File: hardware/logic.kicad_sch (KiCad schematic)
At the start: 42 parts, among them J1 Hanrun HY931147C, SW1 SW_Push, U4 ESP32-WROOM-32E, U5 AMS1117-3.3, U6 LAN8720A

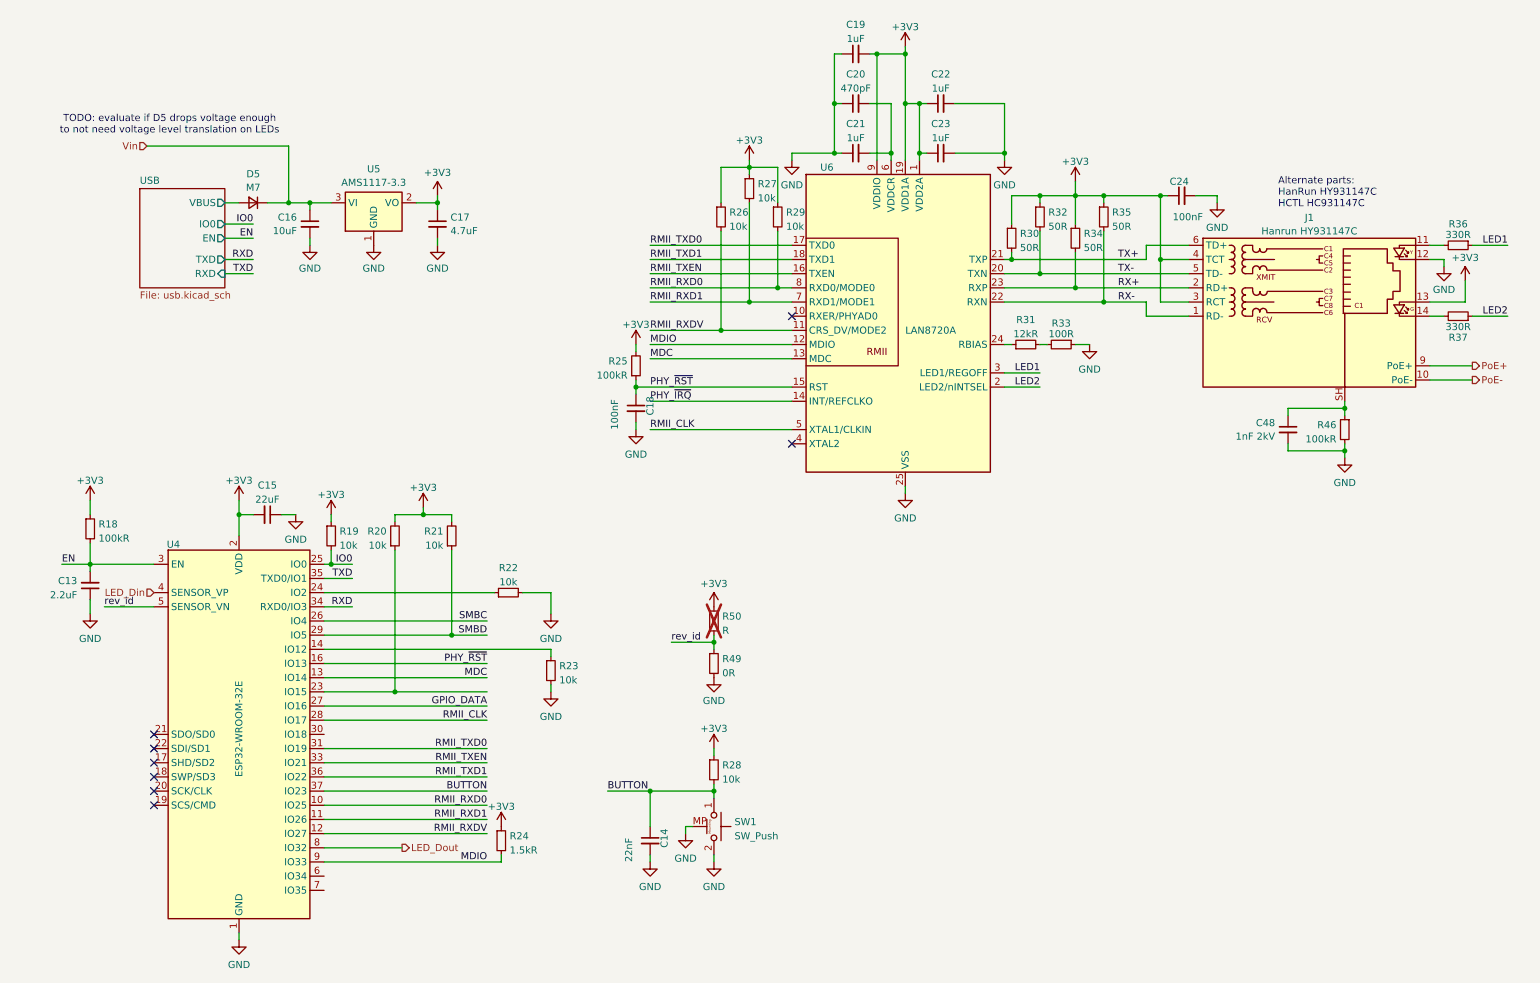
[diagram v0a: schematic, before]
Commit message: hardware: switch to ESP32-C3 MCU and Si3402-B for PoE
Further changes:
 - Enlarge center hole to 16mm diameter
 - Replace Ethernet Phy by KSZ8851 SPI MAC + Phy
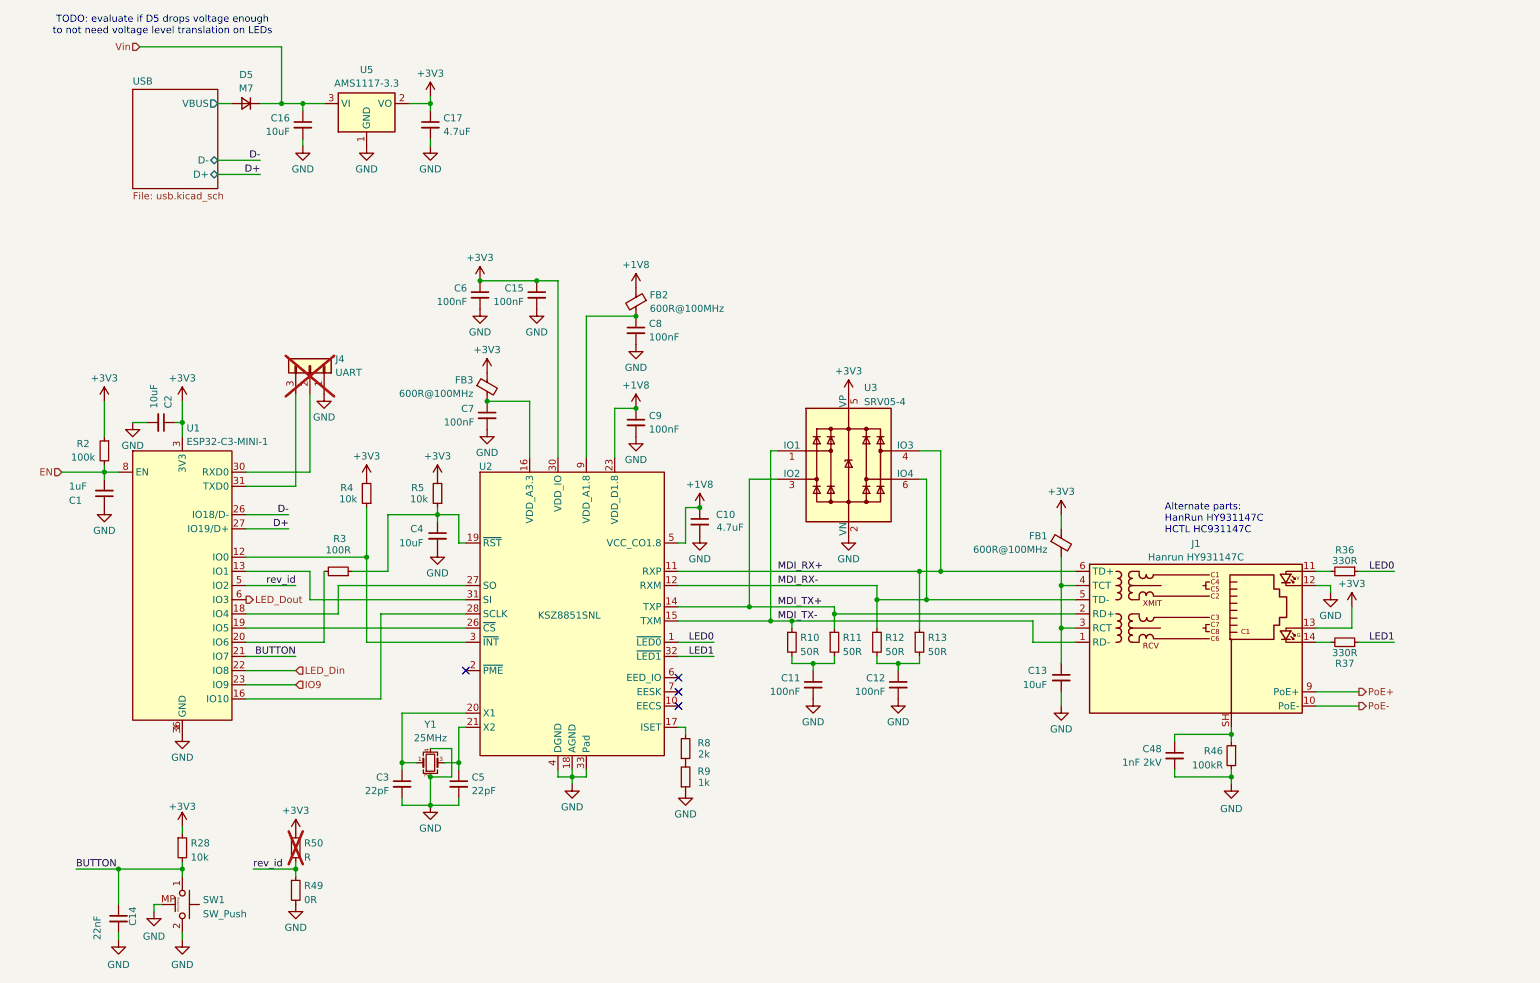
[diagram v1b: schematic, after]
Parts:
- removed C18, C24: 100nF, Capacitor_SMD:C_0402_1005Metric, symbol Device:C_Small
- removed C19, C21, C22, C23: 1uF, Capacitor_SMD:C_0402_1005Metric, symbol Device:C_Small
- removed C20: 470pF, Resistor_SMD:R_0402_1005Metric, symbol Device:C_Small
- removed R18, R25: 100kR, Resistor_SMD:R_0402_1005Metric, symbol Device:R_Small
- removed R19, R20, R21, R22, R23, R26, R27, R29: 10k, Resistor_SMD:R_0402_1005Metric, symbol Device:R_Small
- removed R24: 1.5kR, Resistor_SMD:R_0402_1005Metric, symbol Device:R_Small
- removed R30, R32, R34, R35: 50R, Resistor_SMD:R_0402_1005Metric, symbol Device:R_Small
- removed R31: 12kR, Resistor_SMD:R_0402_1005Metric, symbol Device:R_Small
- removed R33: 100R, Resistor_SMD:R_0402_1005Metric, symbol Device:R_Small
- removed U4: ESP32-WROOM-32E, RF_Module_Espressif:ESP32-WROOM-32E_no_antenna_keepout, symbol RF_Module:ESP32-WROOM-32D
- removed U6: LAN8720A, Package_DFN_QFN:QFN-24-1EP_4x4mm_P0.5mm_EP2.6x2.6mm, symbol Interface_Ethernet:LAN8720A
- added C1: 1uF, Capacitor_SMD:C_0402_1005Metric, symbol Device:C_Small
- added C10: 4.7uF, Capacitor_SMD:C_0402_1005Metric, symbol Device:C_Small
- added C11, C12, C6, C7, C8, C9: 100nF, Capacitor_SMD:C_0402_1005Metric, symbol Device:C_Small
- added C2, C4: 10uF, Capacitor_SMD:C_0402_1005Metric, symbol Device:C_Small
- added C3, C5: 22pF, Capacitor_SMD:C_0402_1005Metric, symbol Device:C_Small
- added FB1, FB2, FB3: 600R@100MHz, Inductor_SMD:L_0402_1005Metric, symbol Device:FerriteBead_Small
- added J4: UART, Connector_PinHeader_2.54mm:PinHeader_1x03_P2.54mm_Vertical, symbol Connector_Generic:Conn_01x03
- added R10, R11, R12, R13: 50R, Resistor_SMD:R_0402_1005Metric, symbol Device:R_Small
- added R2: 100k, Resistor_SMD:R_0402_1005Metric, symbol Device:R_Small
- added R3: 100R, Resistor_SMD:R_0402_1005Metric, symbol Device:R_Small
- added R4, R5: 10k, Resistor_SMD:R_0402_1005Metric, symbol Device:R_Small
- added R8: 2k, Resistor_SMD:R_0402_1005Metric, symbol Device:R_Small
- added R9: 1k, Resistor_SMD:R_0402_1005Metric, symbol Device:R_Small
- added U1: ESP32-C3-MINI-1, ESP32_C3:ESP32-C3-MINI-1, symbol ESP32_C3:ESP32-C3-MINI-1
- added U2: KSZ8851SNL, Package_DFN_QFN:QFN-32-1EP_5x5mm_P0.5mm_EP3.1x3.1mm_ThermalVias, symbol Ethernet_Microchip:KSZ8851SNL
- added U3: SRV05-4, Package_TO_SOT_SMD:SOT-23-6, symbol Power_Protection:SRV05-4
- added Y1: 25MHz, Crystal:Crystal_SMD_3225-4Pin_3.2x2.5mm, symbol Device:Crystal_GND24_Small
- C13: value 2.2uF -> 10uF; footprint Capacitor_SMD:C_0603_1608Metric -> Capacitor_SMD:C_0402_1005Metric; LCSC C23630 -> C15525
- C15: value 22uF -> 100nF; footprint Capacitor_SMD:C_0805_2012Metric -> Capacitor_SMD:C_0402_1005Metric; LCSC C602037 -> C1525
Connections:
- net LED2 is gone; now on net LED1: R37.1
- net +3V3: now also C15.1, C2.1, C6.1, FB1.1, FB3.1, R2.1, R4.2, R5.2, U1.3 (3V3), U2.25 (VDD_IO), U2.30 (VDD_IO), U3.5 (VP); no longer C15.2, J1.3 (RCT), J1.4 (TCT)
- net BUTTON: now also U1.21 (IO7)
- net EN: now also C1.2, R2.2, U1.8 (EN); no longer C13.2
- net LED1: now also U2.32 (~{LED1}); no longer R36.1
- net LED_Din: now also U1.22 (IO8)
- net LED_Dout: now also U1.6 (IO3)
- net rev_id: now also U1.5 (IO2)
- net GND renamed AGND
- net AGND: now also C13.2, C15.2, C1.1, C10.2, C11.2, C12.2, C2.2, C3.2, C4.2, C5.2, C6.2, C7.2, C8.2, C9.2, J4.1 (Pin_1), R9.1, U1.1 (GND), U1.11 (GND), U1.14 (GND), U1.2 (GND), U1.36 (GND), U1.37 (GND), U1.38 (GND), U1.39 (GND), U1.40 (GND), U1.41 (GND), U1.42 (GND), U1.43 (GND), U1.44 (GND), U1.45 (GND), U1.46 (GND), U1.47 (GND), U1.48 (GND), U1.49 (GND), U1.50 (GND), U1.51 (GND), U1.52 (GND), U1.53 (GND), U2.13 (AGND), U2.18 (AGND), U2.22 (DGND), U2.24 (DGND), U2.29 (DGND), U2.33 (Pad), U2.4 (DGND), U2.8 (AGND), U3.2 (VN), Y1.2, Y1.4; no longer C13.1, C15.1
- net RX+ renamed MDI_TX+
- net MDI_TX+: now also R11.1, U2.14 (TXP), U3.3 (IO2)
- net RX- renamed MDI_TX-
- net MDI_TX-: now also R10.1, U2.15 (TXM), U3.1 (IO1)
- net TX+ renamed MDI_RX+
- net MDI_RX+: now also R13.1, U2.11 (RXP), U3.4 (IO3)
- net TX- renamed MDI_RX-
- net MDI_RX-: now also R12.1, U2.12 (RXM), U3.6 (IO4)
- new net: C12.1, R12.2, R13.2
- new net: C8.1, FB2.2, U2.9 (VDD_A1.8)
- new net: J4.2 (Pin_2), U1.30 (RXD0)
- new net: J4.3 (Pin_3), U1.31 (TXD0)
- new net: R4.1, U1.12 (IO0), U2.3 (~{INT})
- new net: C4.1, R3.1, R5.1, U2.19 (~{RST})
- new net: C7.1, FB3.2, U2.16 (VDD_A3.3)
- new net: R8.2, U2.17 (ISET)
- new net: C3.1, U2.20 (X1), Y1.1
- new net: C5.1, U2.21 (X2), Y1.3
- new net: U1.19 (IO5), U2.26 (~{CS})
- new net: U1.18 (IO4), U2.27 (SO)
- new net: U1.16 (IO10), U2.28 (SCLK)
- new net: U1.13 (IO1), U2.31 (SI)
- new net: C11.1, R10.2, R11.2
- new net: R8.1, R9.2
- new net: R3.2, U1.20 (IO6)
- new net: C13.1, FB1.2, J1.3 (RCT), J1.4 (TCT)
- new net +1V8: C10.1, C9.1, FB2.1, U2.23 (VDD_D1.8), U2.5 (VCC_CO1.8)
- new net D+: U1.27 (IO19/D+)
- new net D-: U1.26 (IO18/D-)
- new net IO9: U1.23 (IO9)
- new net LED0: R36.1, U2.1 (~{LED0})
- no-connect marks 8 -> 4
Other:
- sheet USB ports: added D+, D-; removed EN, IO0, RXD, TXD
- moved on the sheet: C14, C16, C17, C48, D5, J1, R28, R36, R37, R46, R49, R50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

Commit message: hardware: replace ESP32-C3 MINI by more common WROOM-02 module
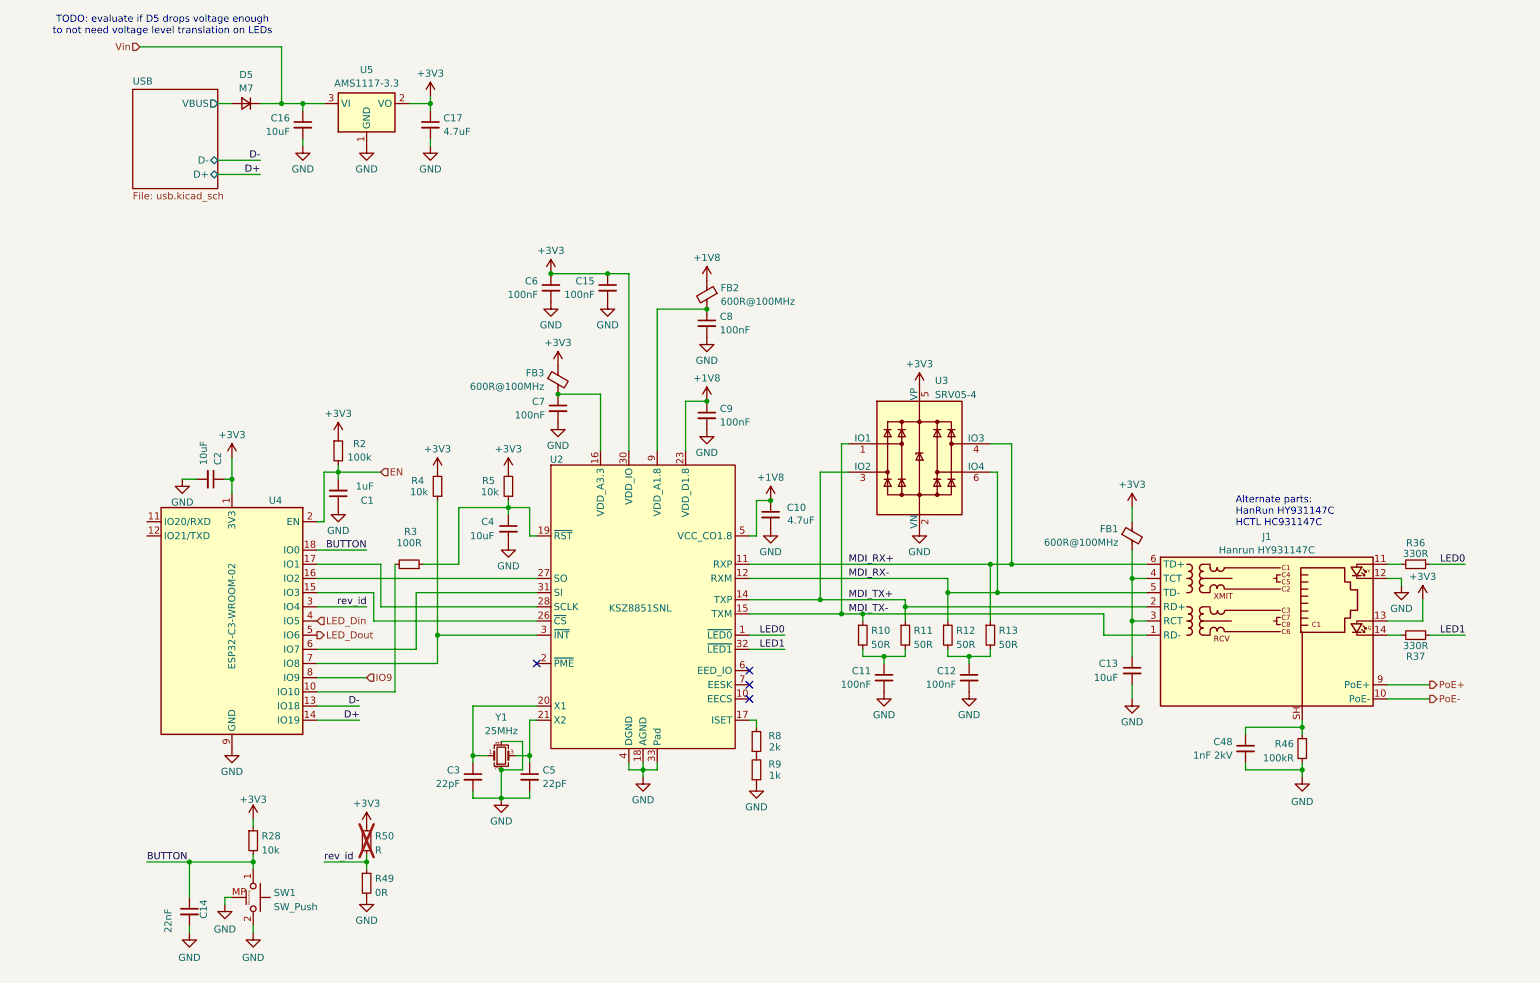
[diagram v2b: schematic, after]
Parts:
- removed J4: UART, Connector_PinHeader_2.54mm:PinHeader_1x03_P2.54mm_Vertical, symbol Connector_Generic:Conn_01x03
- removed U1: ESP32-C3-MINI-1, ESP32_C3:ESP32-C3-MINI-1, symbol ESP32_C3:ESP32-C3-MINI-1
- added U4: ESP32-C3-WROOM-02, RF_Module:ESP32-C3-WROOM-02, symbol RF_Module:ESP32-C3-WROOM-02
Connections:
- net +3V3: now also U4.1 (3V3)
- net AGND: now also U4.19 (GND), U4.9 (GND)
- net BUTTON: now also U4.18 (IO0)
- net D+: now also U4.14 (IO19)
- net D-: now also U4.13 (IO18)
- net EN: now also U4.2 (EN)
- net IO9: now also U4.8 (IO9)
- net LED_Din: now also U4.4 (IO5)
- net LED_Dout: now also U4.5 (IO6)
- net rev_id: now also U4.3 (IO4)
- net at R4.1, U2.3 (~{INT}): now also U4.7 (IO8)
- net at U2.26 (~{CS}): now also U4.15 (IO3)
- net at U2.27 (SO): now also U4.16 (IO2)
- net at U2.28 (SCLK): now also U4.17 (IO1)
- net at U2.31 (SI): now also U4.6 (IO7)
- net at R3.2: now also U4.10 (IO10)
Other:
- moved on the sheet: C1, C10, C11, C12, C13, C14, C15, C2, C3, C4, C48, C5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

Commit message: hardware: add testpoints to flyback converter and SPI MAC + Phy
Add testpoints to all critical section that might require in-circuit
debugging
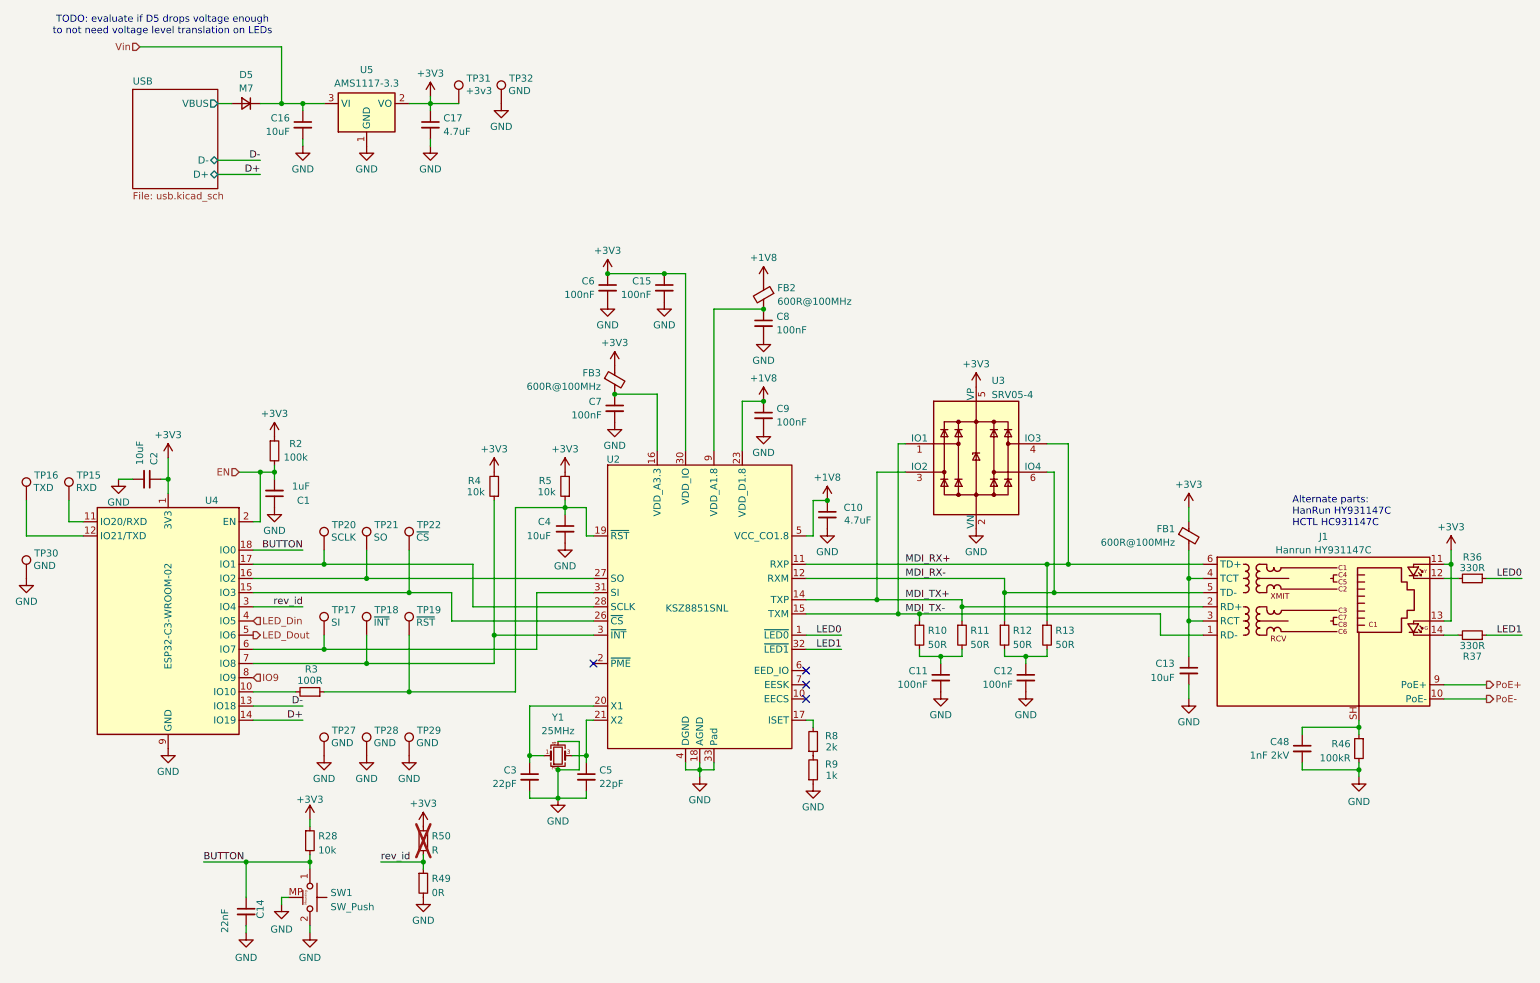
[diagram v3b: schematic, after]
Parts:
- added TP15: RXD, TestPoint_no_outline:TestPoint_Pad_D2.0mm_no_outline, symbol Connector:TestPoint
- added TP16: TXD, TestPoint_no_outline:TestPoint_Pad_D2.0mm_no_outline, symbol Connector:TestPoint
- added TP17: SI, TestPoint_no_outline:TestPoint_Pad_D2.0mm_no_outline, symbol Connector:TestPoint
- added TP18: ~{INT}, TestPoint_no_outline:TestPoint_Pad_D2.0mm_no_outline, symbol Connector:TestPoint
- added TP19: ~{RST}, TestPoint_no_outline:TestPoint_Pad_D2.0mm_no_outline, symbol Connector:TestPoint
- added TP20: SCLK, TestPoint_no_outline:TestPoint_Pad_D2.0mm_no_outline, symbol Connector:TestPoint
- added TP21: SO, TestPoint_no_outline:TestPoint_Pad_D2.0mm_no_outline, symbol Connector:TestPoint
- added TP22: ~{CS}, TestPoint_no_outline:TestPoint_Pad_D2.0mm_no_outline, symbol Connector:TestPoint
- added TP27, TP28, TP29, TP30, TP32: GND, TestPoint:TestPoint_Pad_D2.0mm, symbol Connector:TestPoint
- added TP31: +3v3, TestPoint_no_outline:TestPoint_Pad_D2.0mm_no_outline, symbol Connector:TestPoint
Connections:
- net +3V3: now also J1.11, TP31.1
- net AGND: now also TP27.1, TP28.1, TP29.1, TP30.1, TP32.1; no longer J1.12
- net at R4.1, U2.3 (~{INT}), U4.7 (IO8): now also TP18.1
- net at U4.11 (IO20/RXD): now also TP15.1
- net at U4.12 (IO21/TXD): now also TP16.1
- net at U2.26 (~{CS}), U4.15 (IO3): now also TP22.1
- net at U2.27 (SO), U4.16 (IO2): now also TP21.1
- net at U2.28 (SCLK), U4.17 (IO1): now also TP20.1
- net at U2.31 (SI), U4.6 (IO7): now also TP17.1
- net at C4.1, R3.1, R5.1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: now also TP19.1
- net at R36.2: now also J1.12; no longer J1.11
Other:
- moved on the sheet: C1, C10, C11, C12, C13, C14, C15, C2, C3, C4, C48, C5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
